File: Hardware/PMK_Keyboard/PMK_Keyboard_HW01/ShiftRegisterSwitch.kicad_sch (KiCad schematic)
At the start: 50 parts, among them SW501 SW_Push, SW502 SW_Push, SW503 SW_Push, SW504 SW_Push, SW505 SW_Push, SW506 SW_Push, SW507 SW_Push, SW508 SW_Push, SW509 SW_Push, SW510 SW_Push, SW511 SW_Push, SW512 SW_Push, SW513 SW_Push, SW514 SW_Push, SW515 SW_Push, SW516 SW_Push, SW517 SW_Push, SW518 SW_Push, SW519 SW_Push, SW520 SW_Push, SW521 SW_Push, SW522 SW_Push, SW523 SW_Push, SW524 SW_Push, SW525 SW_Push, SW526 SW_Push, SW527 SW_Push, SW528 SW_Push, SW529 SW_Push, SW530 SW_Push, SW531 SW_Push, SW532 SW_Push, SW533 SW_Push, SW534 SW_Push, SW535 SW_Push, SW536 SW_Push, SW537 SW_Push, SW538 SW_Push, SW539 SW_Push, SW540 SW_Push, U501 SN74HC165PWR, U502 SN74HC165PWR, U503 SN74HC165PWR, U504 SN74HC165PWR, U505 SN74HC165PWR

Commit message: Started routing
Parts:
- removed RN505: EXB-2HV103JV, Component_lib:EXB2HV_1, symbol Component lib:EXB-2HV103JV
- removed SW530, SW531, SW532, SW533, SW534, SW535, SW536, SW537, SW538, SW539, SW540: SW_Push, Component_lib:Kailh_socket_PG1350_reversible, symbol Switch:SW_Push
- removed U505: SN74HC165PWR, Component_lib:SOP65P640X120-16N, symbol Component_lib:SN74HC165PWR
- added SW301: RIC11-22S10D5S-TH, Component_lib:RIC11-22S10D5S-TH, symbol Component_lib:RIC11-22S10D5S-TH
- SW302: renamed from SW501; footprint Component_lib:SKRPABE010 -> Component_lib:Kailh_socket_PG1350_reversible
- renumbered RN501 to RN301, RN502 to RN302, RN503 to RN303, RN504 to RN304, SW502 to SW303, SW503 to SW304, SW504 to SW305, SW505 to SW306, SW506 to SW307, SW507 to SW308, SW508 to SW309, SW509 to SW310, SW510 to SW311, SW511 to SW312, SW512 to SW313, SW513 to SW314, SW514 to SW315, SW515 to SW316, SW516 to SW317, SW517 to SW318, SW518 to SW319, SW519 to SW320, SW520 to SW321, SW521 to SW322, SW522 to SW323, SW523 to SW324, SW524 to SW325, SW525 to SW326, SW526 to SW327, SW527 to SW328, SW528 to SW329, SW529 to SW330, U501 to U301, U502 to U302, U503 to U303, U504 to U304
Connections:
- net 30: now also SW301.S1
- net GND: now also SW301.C, SW301.S2
- net 4-5: no longer names the net of U304.10 (SER)
- new net A: SW301.A
- new net B: SW301.B
- no-connect marks 6 -> 4
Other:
- note added: "300- Shift Register - Switch"
- note removed: "500- Shift Register - Switch"

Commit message: working on routing
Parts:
- removed SW301: RIC11-22S10D5S-TH, Component_lib:RIC11-22S10D5S-TH, symbol Component_lib:RIC11-22S10D5S-TH
- added SW330: RIC11-22S10D5S-TH, Component_lib:RIC11-22S10D5S-TH, symbol Component_lib:RIC11-22S10D5S-TH
- renumbered SW302 to SW301, SW303 to SW302, SW304 to SW303, SW305 to SW304, SW306 to SW305, SW307 to SW306, SW308 to SW307, SW309 to SW308, SW310 to SW309, SW311 to SW310, SW312 to SW311, SW313 to SW312, SW314 to SW313, SW315 to SW314, SW316 to SW315, SW317 to SW316, SW318 to SW317, SW319 to SW318, SW320 to SW319, SW321 to SW320, SW322 to SW321, SW323 to SW322, SW324 to SW323, SW325 to SW324, SW326 to SW325, SW327 to SW326, SW328 to SW327, SW329 to SW328, SW330 to SW329
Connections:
- net 30: now also SW330.S1
- net A: now also SW330.A
- net B: now also SW330.B
- net GND: now also SW330.C, SW330.S2

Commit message: Routing still going on
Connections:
- net 30: now also SW330.S2; no longer SW330.S1
- net GND: now also SW330.S1; no longer SW330.S2
- no-connect marks 4 -> 5
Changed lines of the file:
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@@
   (no_connect (at 53.34 137.16))
   (no_connect (at 243.84 137.16))
+  (no_connect (at 279.4 137.16))
   (no_connect (at 116.84 137.16))
   (wire (pts (xy 205.74 205.74) (xy 205.74 213.36))
@@
     (effects (font (size 1.27 1.27)) (justify right bottom))
   )
-  (label "A" (at 292.1 203.2 180) (fields_autoplaced)
+  (label "A" (at 292.1 208.28 180) (fields_autoplaced)
     (effects (font (size 1.27 1.27)) (justify right bottom))
   )
@@
     (effects (font (size 1.27 1.27)) (justify left bottom))
   )
-  (label "B" (at 292.1 208.28 180) (fields_autoplaced)
+  (label "B" (at 292.1 203.2 180) (fields_autoplaced)
     (effects (font (size 1.27 1.27)) (justify right bottom))
   )
@@
     )
   )
-  (symbol (lib_id "Component_lib:RIC11-22S10D5S-TH") (at 304.8 205.74 0) (unit 1)
-    (in_bom yes) (on_board yes) (dnp no) (fields_autoplaced)
-    (property "Reference" "SW330" (at 304.8 197.6501 0)
-      (effects (font (size 1.27 1.27)))
-    )
-    (property "Value" "RIC11-22S10D5S-TH" (at 304.8 199.5711 0)
-      (effects (font (size 1.27 1.27)))
-    )
-    (property "Footprint" "Component_lib:RIC11-22S10D5S-TH" (at 300.99 201.676 0)
-      (effects (font (size 1.27 1.27)) hide)
-    )
-    (property "Datasheet" "https://www.mouser.ch/ProductDetail/CUI-Devices/RIC11-22S10D5S-TH?qs=HoCaDK9Nz5fxypdms%252BmQUg%3D%3D" (at 304.8 199.136 0)
-      (effects (font (size 1.27 1.27)) hide)
-    )
+  (symbol (lib_id "Component_lib:RIC11-22S10D5S-TH") (at 304.8 205.74 0) (mirror x) (unit 1)
+    (in_bom yes) (on_board yes) (dnp no)
+    (property "Reference" "SW330" (at 304.8 195.58 0)
+      (effects (font (size 1.27 1.27)))
+    )
+    (property "Value" "RIC11-22S10D5S-TH" (at 304.8 198.12 0)
+      (effects (font (size 1.27 1.27)))
+    )
+    (property "Footprint" "Component_lib:RIC11-22S10D5S-TH" (at 300.99 209.804 0)
+      (effects (font (size 1.27 1.27)) hide)
+    )
+    (property "Datasheet" "https://www.mouser.ch/ProductDetail/CUI-Devices/RIC11-22S10D5S-TH?qs=HoCaDK9Nz5fxypdms%252BmQUg%3D%3D" (at 304.8 212.344 0)
+      (effects (font (size 1.27 1.27)) hide)
+    )

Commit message: a bit of routing
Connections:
- net GND: now also SW330.MP
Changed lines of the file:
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@@
+    (stroke (width 0) (type default))
+  )
+  (wire (pts (xy 312.42 208.28) (xy 317.5 208.28))
     (stroke (width 0) (type default))
   )
@@
     (stroke (width 0) (type default))
   )
-  (wire (pts (xy 314.96 210.82) (xy 314.96 208.28))
-    (stroke (width 0) (type default))
-  )
   (wire (pts (xy 223.52 167.64) (xy 223.52 170.18))
     (stroke (width 0) (type default))
@@
     (stroke (width 0) (type default))
   )
+  (wire (pts (xy 314.96 203.2) (xy 314.96 210.82))
+    (stroke (width 0) (type default))
+  )
   (wire (pts (xy 33.02 170.18) (xy 35.56 170.18))
     (stroke (width 0) (type default))
@@
   )
   (wire (pts (xy 152.4 132.08) (xy 185.42 132.08))
-    (stroke (width 0) (type default))
-  )
-  (wire (pts (xy 314.96 208.28) (xy 312.42 208.28))
     (stroke (width 0) (type default))
   )
@@
     (effects (font (size 1.27 1.27)) (justify right bottom))
   )
-  (label "A" (at 292.1 208.28 180) (fields_autoplaced)
+  (label "A" (at 292.1 203.2 180) (fields_autoplaced)
     (effects (font (size 1.27 1.27)) (justify right bottom))
   )
@@
     (effects (font (size 1.27 1.27)) (justify left bottom))
   )
-  (label "B" (at 292.1 203.2 180) (fields_autoplaced)
+  (label "B" (at 292.1 208.28 180) (fields_autoplaced)
     (effects (font (size 1.27 1.27)) (justify right bottom))
   )
@@
     (effects (font (size 1.27 1.27)) (justify right bottom))
   )
-  (label "30" (at 314.96 203.2 0) (fields_autoplaced)
+  (label "30" (at 317.5 208.28 0) (fields_autoplaced)
     (effects (font (size 1.27 1.27)) (justify left bottom))
   )
@@
     )
   )
+  (symbol (lib_id "power:GND") (at 304.8 213.36 0) (unit 1)
+    (in_bom yes) (on_board yes) (dnp no) (fields_autoplaced)
+    (property "Reference" "#PWR0321" (at 304.8 219.71 0)
+      (effects (font (size 1.27 1.27)) hide)
+    )
+    (property "Value" "GND" (at 304.8 217.8034 0)
+      (effects (font (size 1.27 1.27)))
+    )
+    (property "Footprint" "" (at 304.8 213.36 0)
+      (effects (font (size 1.27 1.27)) hide)
+    )
+    (property "Datasheet" "" (at 304.8 213.36 0)
+      (effects (font (size 1.27 1.27)) hide)
+    )
+    (pin "1")
+    (instances
+      (project "PMK_Keyboard_HW01"
+        (path "/c3b08055-08a5-4979-9bf8-f36ab0917722/2ae89e7d-b59a-451e-9e36-5967d907d91f"
+          (reference "#PWR0321") (unit 1)
+        )
+      )
+    )
+  )
   (symbol (lib_id "power:+3V3") (at 223.52 165.1 0) (unit 1)
     (in_bom yes) (on_board yes) (dnp no) (fields_autoplaced)
@@
     )
   )
-  (symbol (lib_id "Component_lib:RIC11-22S10D5S-TH") (at 304.8 205.74 0) (mirror x) (unit 1)
+  (symbol (lib_id "Component_lib:RIC11-22S10D5S-TH") (at 304.8 205.74 0) (unit 1)
     (in_bom yes) (on_board yes) (dnp no)
     (property "Reference" "SW330" (at 304.8 195.58 0)
@@
       (effects (font (size 1.27 1.27)))
     )
-    (property "Footprint" "Component_lib:RIC11-22S10D5S-TH" (at 300.99 209.804 0)
-      (effects (font (size 1.27 1.27)) hide)
-    )
-    (property "Datasheet" "https://www.mouser.ch/ProductDetail/CUI-Devices/RIC11-22S10D5S-TH?qs=HoCaDK9Nz5fxypdms%252BmQUg%3D%3D" (at 304.8 212.344 0)
+    (property "Footprint" "Component_lib:RIC11-22S10D5S-TH" (at 300.99 201.676 0)
+      (effects (font (size 1.27 1.27)) hide)
+    )
+    (property "Datasheet" "https://www.mouser.ch/ProductDetail/CUI-Devices/RIC11-22S10D5S-TH?qs=HoCaDK9Nz5fxypdms%252BmQUg%3D%3D" (at 304.8 199.136 0)
       (effects (font (size 1.27 1.27)) hide)
     )
@@
     (pin "B")
     (pin "C")
+    (pin "MP")
     (pin "S1")
     (pin "S2")

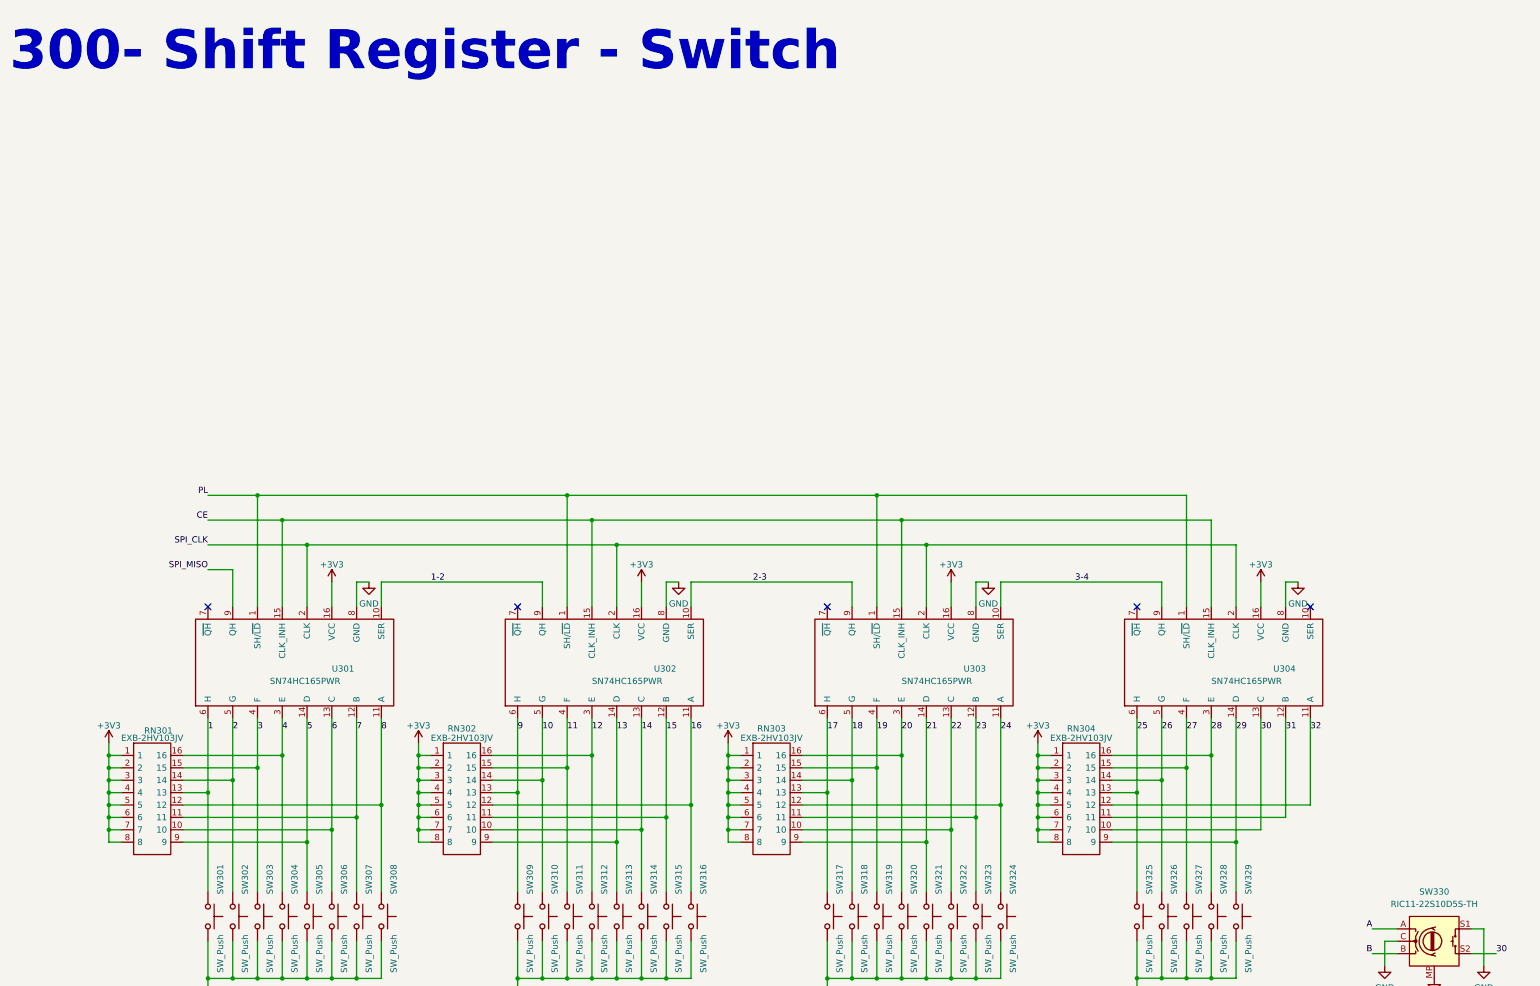
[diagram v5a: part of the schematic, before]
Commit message: added mounting holes + fix in ref des
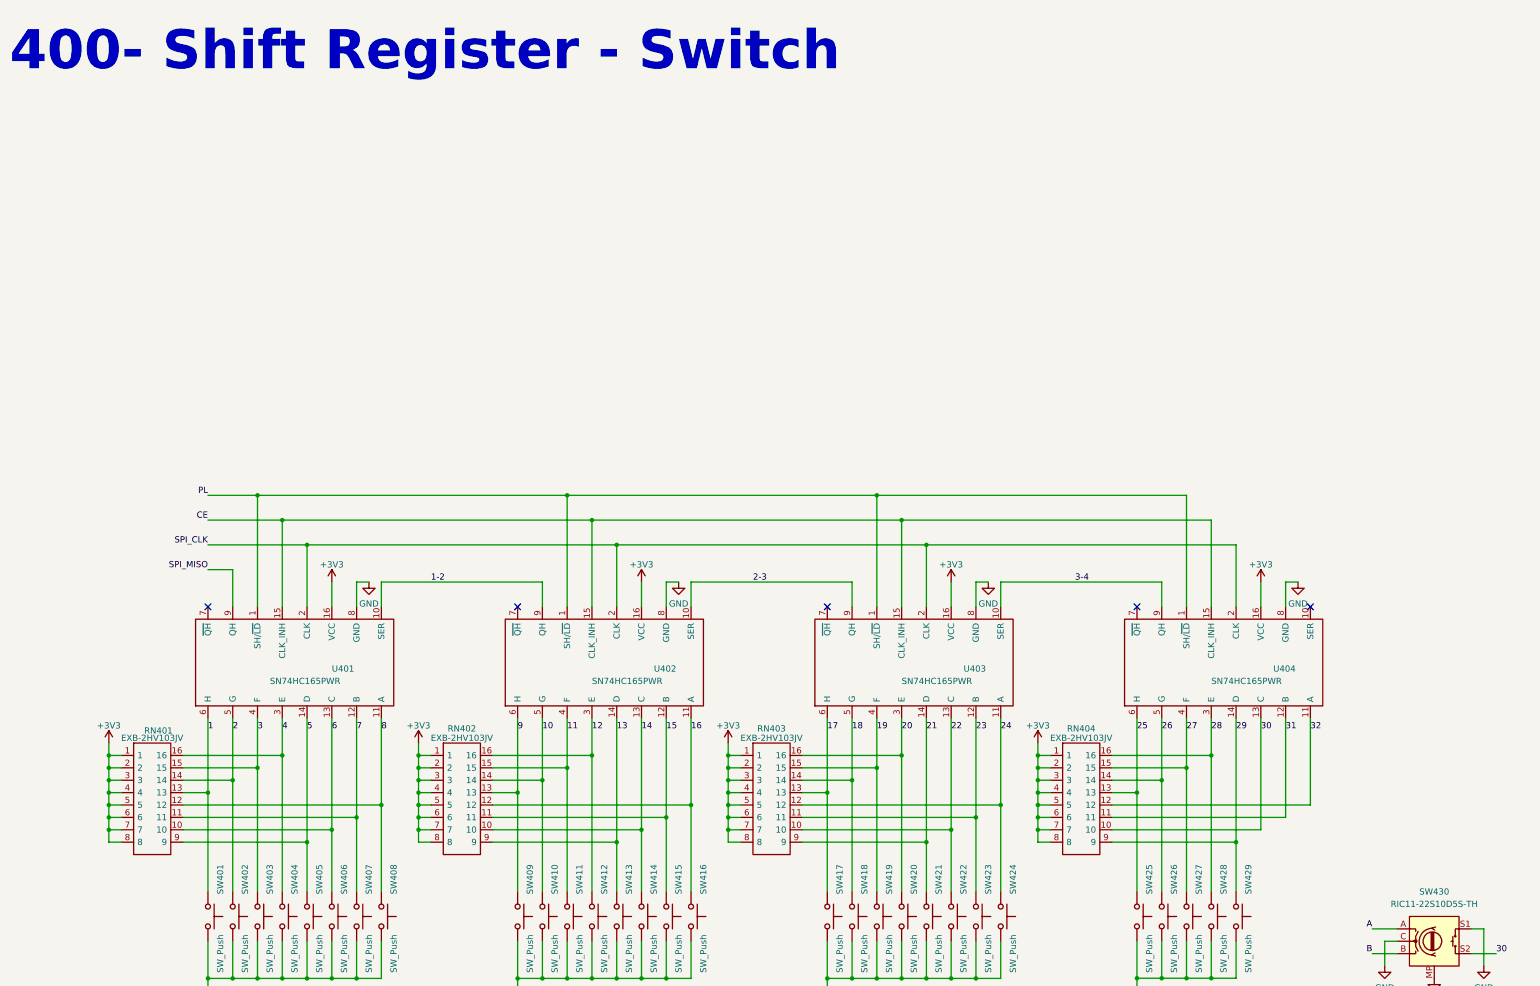
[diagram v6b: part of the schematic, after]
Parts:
- renumbered RN301 to RN401, RN302 to RN402, RN303 to RN403, RN304 to RN404, SW301 to SW401, SW302 to SW402, SW303 to SW403, SW304 to SW404, SW305 to SW405, SW306 to SW406, SW307 to SW407, SW308 to SW408, SW309 to SW409, SW310 to SW410, SW311 to SW411, SW312 to SW412, SW313 to SW413, SW314 to SW414, SW315 to SW415, SW316 to SW416, SW317 to SW417, SW318 to SW418, SW319 to SW419, SW320 to SW420, SW321 to SW421, SW322 to SW422, SW323 to SW423, SW324 to SW424, SW325 to SW425, SW326 to SW426, SW327 to SW427, SW328 to SW428, SW329 to SW429, SW330 to SW430, U301 to U401, U302 to U402, U303 to U403, U304 to U404
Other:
- note added: "400- Shift Register - Switch"
- note removed: "300- Shift Register - Switch"
